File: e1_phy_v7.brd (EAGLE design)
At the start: 100 x 75 mm, 127 parts, among them IC2 LD117AS33TR, IC3 LD117AS33TR, U1 IDT82V2081, U2 GPS_GNS_2201, U3 VCTCXO-CONNORWINFIELD, U4 VCXO_TAITIEN_VT, U5 IP4234CZ6, U7 IP4234CZ6, X2 SMA-142-0701-801/806, X3 JACK2.5_SJ-2523, X4 0446200002

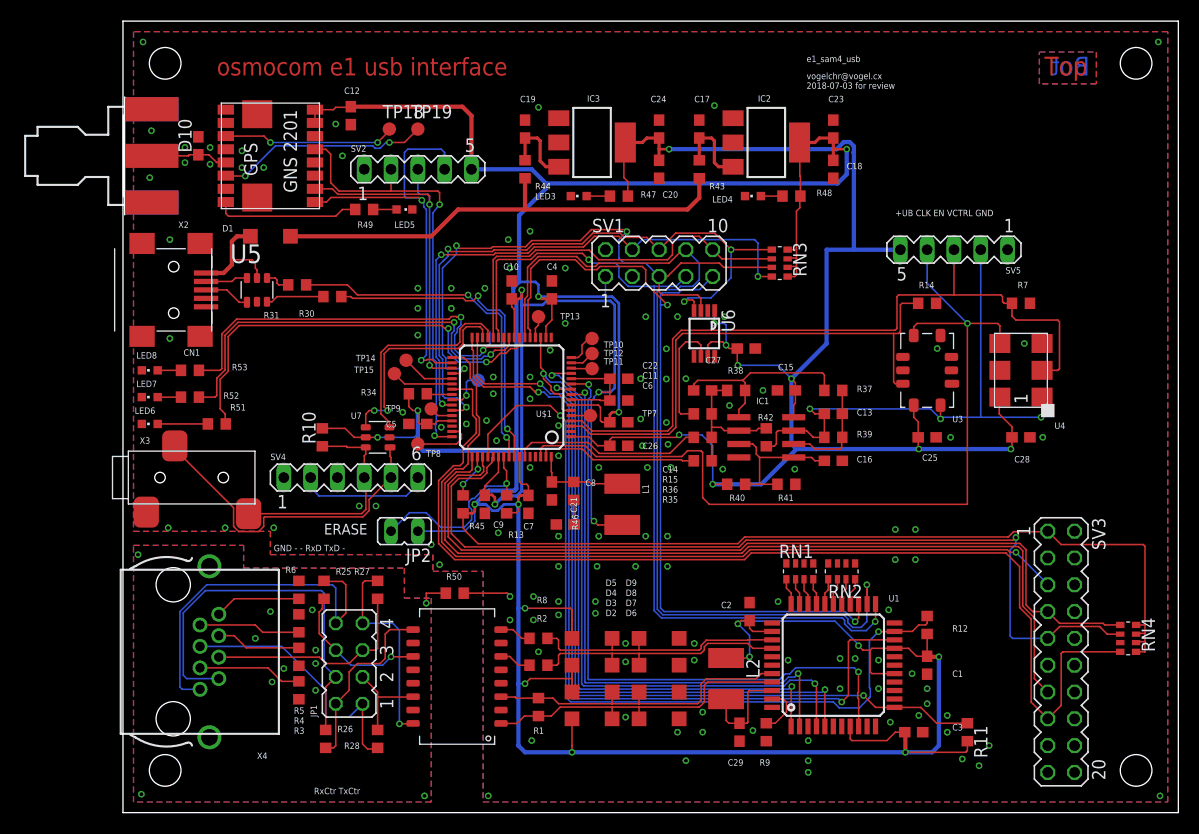
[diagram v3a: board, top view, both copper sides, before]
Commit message: Testpads for unused LIU signals.
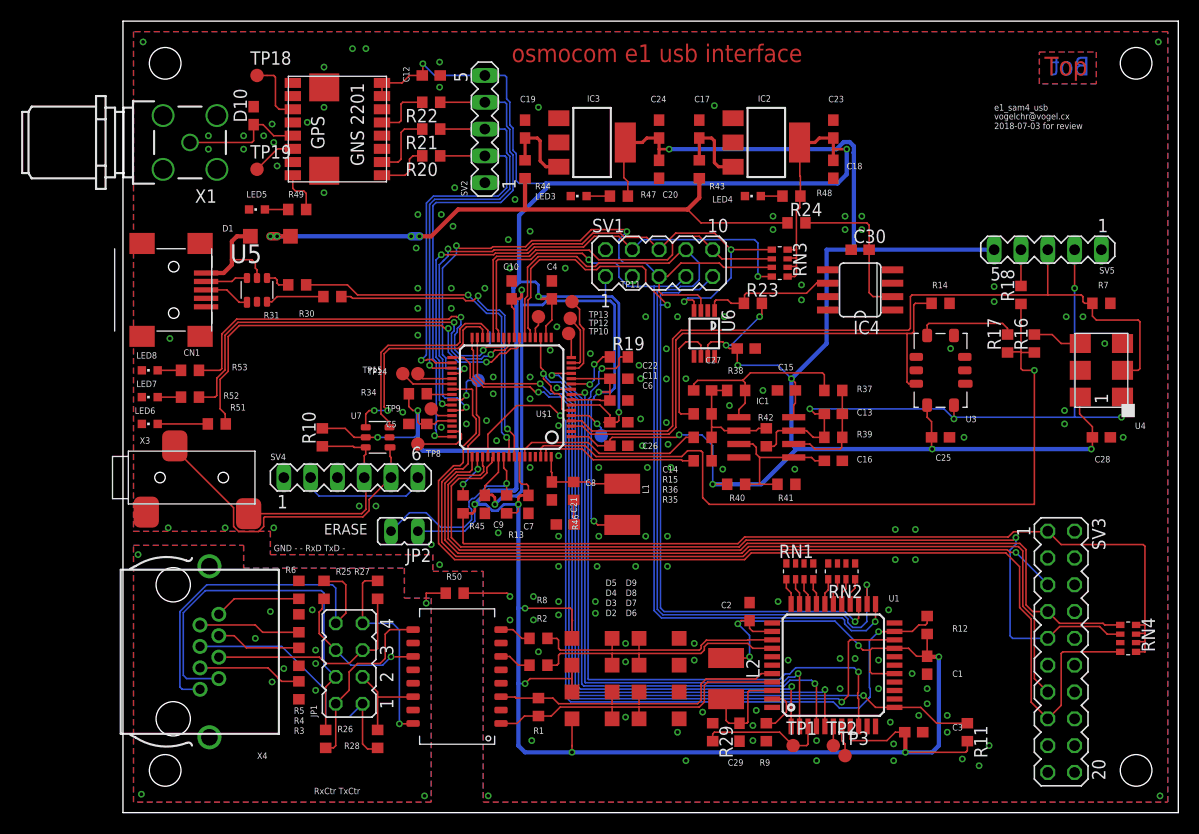
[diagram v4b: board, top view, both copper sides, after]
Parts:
- removed X2: SMA-142-0701-801/806, con-coax:J502-ND-142-0701-801/806
- added C30: 100n, rcl:C0603
- added IC4: MAX6173AASA, maxim:SO08
- added R16, R17, R18, R19, R20, R21, R22: 33R, rcl:R0603
- added R23: 0R (DNP), rcl:R0603
- added R24: BLM/0R, rcl:R0603
- added R29: 10k, rcl:R0603
- added TP1, TP2, TP3: TPB1,27, testpad:B1,27
- added X1: BU-SMA-G, con-coax:BU-SMA-G
- moved TP19 15.7 mm to (12.7, 61.0)
- moved LED5 14.0 mm to (12.7, 57.1), turned to 90 degrees
- moved TP18 13.5 mm to (12.7, 69.8)
- moved SV5 8.89 mm to (87.6, 53.3)
- moved C12 8.52 mm to (29.2, 69.8), turned to 0 degrees
- moved C28 7.62 mm to (92.7, 35.6)
- moved R7 7.62 mm to (92.7, 48.3)
- moved U4 7.62 mm to (92.7, 41.9)
- moved SV2 7.41 mm to (34.3, 64.8), turned to 90 degrees
- moved U2 6.84 mm to (20.3, 64.8)
- moved TP11 6.63 mm to (42.5, 48.4)
- moved R49 6.35 mm to (16.5, 57.1), turned to 0 degrees
- moved D10 5.97 mm to (12.4, 66.0)
- moved TP12 3.92 mm to (42.4, 46.8)
- moved TP10 2.27 mm to (42.2, 45.4)
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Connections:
- net N$10 renamed GPS_3DFIX
- net N$19 renamed TP12
- net N$20 renamed TP13
- net N$21 renamed TP7
- net N$22 renamed TP14
- net N$23 renamed TP15
- net N$24 renamed GPS_WAKEUP
- net N$6 renamed TP9
- net N$7 renamed TP8
- net N$8 renamed TP10
- net N$9 renamed TP11
- new net CLK2048_SAM4S: R19.1, U$1.11
- new net GPS_RF: D10.1, U2.5, X1.1
- new net GPS_RX_A: R20.2, U2.9
- new net N$30: R22.2, U2.13
- new net N$6: R29.2, TP1.TP, U1.3
- new net N$7: IC4.6, R23.1, U6.1
- new net N$8: TP3.TP, U1.7
- new net N$9: C30.2, IC4.2, R24.2
- new net SAM4S_CLK_EXT: R18.2, SV5.4
- new net SAM4S_CLK_VCTXO: R17.2, U3.5
- new net SAM4S_CLK_VCXO: R16.2, U4.4
- new net TPS_TX_A: R21.2, U2.10
- net +UB: now also R23.2; no longer U6.1
- net CLK2048: now also R19.2; no longer U$1.11
- net GND: now also C30.1, IC4.4, R29.1, X1.2, X1.3, X1.4, X1.5; no longer U1.3, X2.G@1, X2.G@2, X2.G@3, X2.G@4
- net GPS_PPS: now also R22.1, SV2.4; no longer SV2.2, U2.13
- net GPS_SAM4_RX: now also R21.1; no longer U2.10
- net GPS_SAM4_TX: now also R20.1, SV2.2; no longer SV2.4, U2.9
- net N$4: now also TP2.TP, U1.6; no longer D10.1, U2.5, X2.1
- net SAM4S_CLK: now also R16.1, R17.1, R18.1; no longer SV5.4, U3.5, U4.4
- net USB_VBUS: now also R24.1
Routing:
- net +UB: track 146.1 -> 163.9 mm
- net GPS_WAKEUP: track 20.3 -> 4.20 mm, vias 2 -> 0
- net N$9: track 0.00 -> 14.9 mm
- net USB_VBUS: track 45.1 -> 58.2 mm, vias 0 -> 4
- net N$7: track 0.00 -> 13.0 mm
- net N$6: track 0.00 -> 12.1 mm
- net GPS_RF: track 0.00 -> 11.8 mm
- net #GPS_RESET: track 16.4 -> 6.30 mm, vias 2 -> 0
- net GPS_3DFIX: track 13.7 -> 4.23 mm
- net SAM4S_CLK_VCTXO: track 0.00 -> 9.45 mm
- net VCXO_CTRL: track 52.3 -> 60.1 mm, vias 3 -> 4
- net VCXO_EN: track 71.1 -> 78.7 mm
- net SAM4S_CLK: track 83.2 -> 75.7 mm
- net TPS_TX_A: track 0.00 -> 6.60 mm
- net TP11: track 1.99 -> 7.71 mm
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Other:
- board text removed: "+UB CLK EN VCTRL GND"

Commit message: Cleaned up silkscreen.
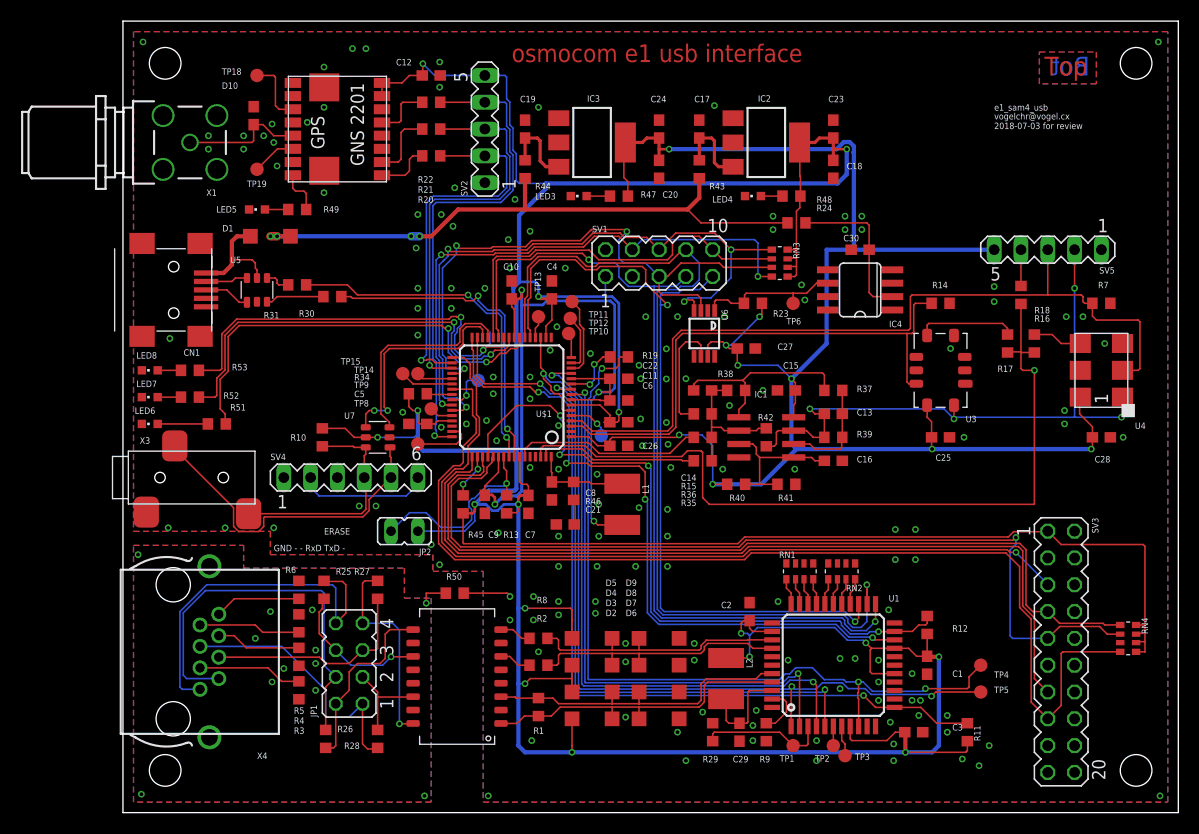
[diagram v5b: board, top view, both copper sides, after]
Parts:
- added TP4, TP5, TP6: TPB1,27, testpad:B1,27
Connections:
- net CLK2048: now also TP4.TP
- net N$7: now also TP6.TP
- net TX_CLK: now also TP5.TP
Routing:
- net TX_CLK: track 64.6 -> 83.6 mm, vias 2 -> 3
- net #SPI_CS1: track 79.3 -> 65.6 mm, vias 2 -> 4
- net CLK2048: track 64.8 -> 77.7 mm, vias 2 -> 3
- net #LIU_INT: track 78.0 -> 65.4 mm, vias 2 -> 4
- net VCC: track 432.6 -> 431.4 mm
- net N$7: track 13.0 -> 13.9 mm
- net GND: vias 154 -> 156
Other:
- board text removed: "RxCtr TxCtr"

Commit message: Some cleanup before declaring final.
ADVREF of SAM4S fed by VREF net.
+UB/2 divider fed by VREF net, renamed to VREF_HALF.
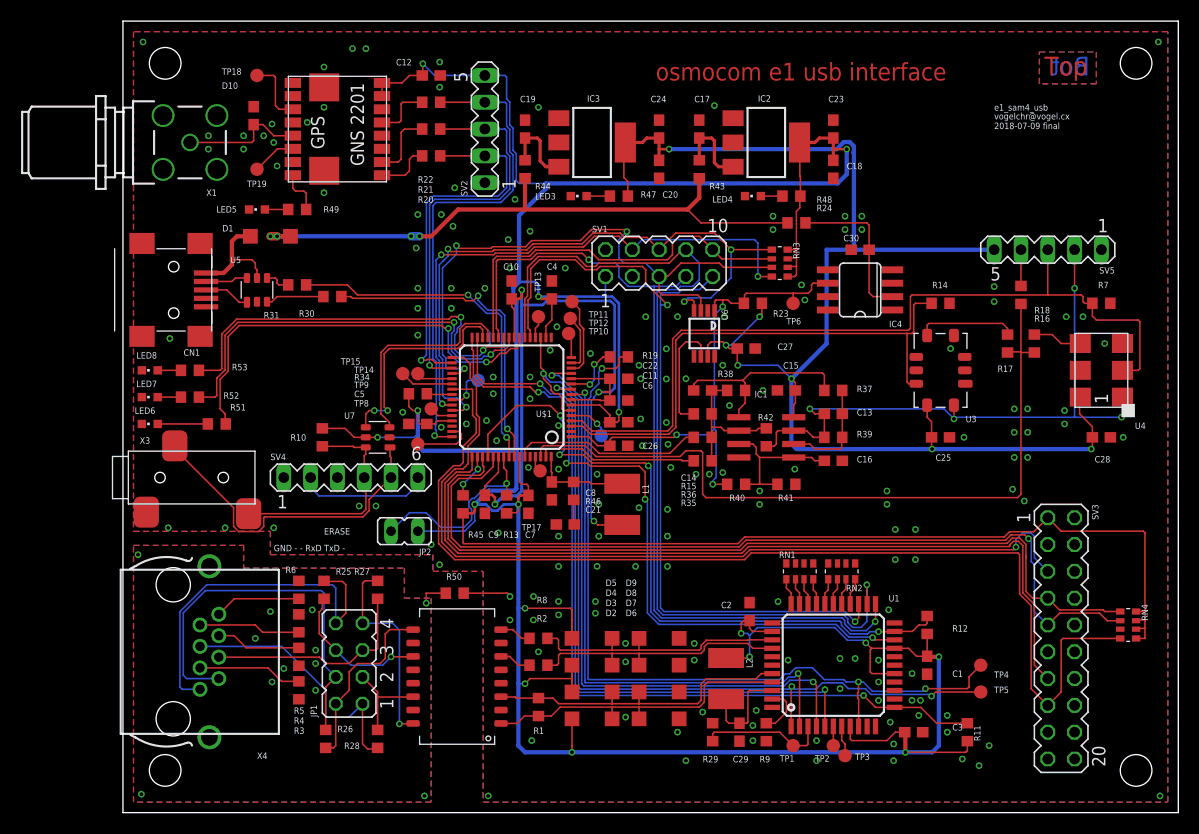
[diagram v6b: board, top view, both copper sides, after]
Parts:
- added TP17: TPB1,27, testpad:B1,27
- moved SV3 1.27 mm to (88.9, 16.5)
- moved RN4 1.27 mm to (95.2, 17.8)
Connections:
- net +UB_HALF renamed VREF_HALF
- removed net N$7: IC4.6, R23.1, TP6.TP, U6.1
- new net TP17: TP17.TP, U$1.61
- new net VREF: C26.2, IC4.6, R23.1, R40.1, TP6.TP, U$1.1, U6.1
- net +UB: no longer C26.2, R40.1, U$1.1
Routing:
- net VREF: track 0.00 -> 48.5 mm, vias 0 -> 3
- net +UB: track 163.9 -> 134.7 mm, vias 9 -> 7
- net N$7: track 13.9 -> 0.00 mm
- net SAM4S_CLK: track 75.7 -> 72.0 mm, vias 1 -> 0
- net TCK_SWDCLK: track 85.6 -> 82.8 mm
- net TDI: track 80.8 -> 83.2 mm
- net TP17: track 0.00 -> 1.52 mm
- net VCC: track 431.4 -> 432.0 mm
- net #RESET: track 102.9 -> 102.3 mm
- net TMS_SWDIO: track 81.1 -> 80.6 mm
- net TDO: track 79.8 -> 79.3 mm
- net GND: vias 156 -> 171
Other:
- board text added: "vogelchr@vogel.cx 2018-07-09 final"
- board text removed: "vogelchr@vogel.cx 2018-07-03 for review"
